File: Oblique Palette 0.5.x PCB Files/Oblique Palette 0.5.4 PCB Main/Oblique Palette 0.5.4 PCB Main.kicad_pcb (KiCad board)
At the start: 2 copper layers, 235 x 110 mm, 301 parts, among them J11 Conn_01x03_Male_Pin, J13 Conn_01x03_Male_Pin, J14 Conn_01x03_Male_Pin, J16 Conn_01x03_Female_Pin, J17 AudioJack2_SwitchT, J19 Conn_01x03_Female_Pin, J2 Conn_01x03_Male_Pin, J20 AudioJack2_SwitchT, J22 Conn_01x03_Female_Pin, J23 AudioJack2_SwitchT, J25 Conn_01x03_Female_Pin, J26 AudioJack2_SwitchT, J28 Conn_01x03_Female_Pin, J29 AudioJack2_SwitchT, J31 Conn_01x03_Female_Pin, J32 AudioJack2_SwitchT, J34 Conn_01x03_Female_Pin, J35 AudioJack2_SwitchT, J37 Conn_01x03_Female_Pin, J38 AudioJack2_SwitchT, J4 Conn_01x03_Male_Pin, J40 Conn_01x03_Female_Pin, J42 AudioJack2_SwitchT, J44 Conn_01x03_Female_Pin, J46 AudioJack2_SwitchT, J48 Conn_01x03_Female_Pin, J5 Conn_01x03_Male_Pin, J50 AudioJack2_SwitchT, J52 Conn_01x03_Female_Pin, J54 AudioJack2_SwitchT, J56 Conn_01x03_Female_Pin, J58 AudioJack2_SwitchT, J60 Conn_01x03_Female_Pin, J62 AudioJack2_SwitchT, J64 Conn_01x03_Female_Pin, J66 AudioJack2_SwitchT, J68 Conn_01x03_Female_Pin, J7 Conn_01x03_Male_Pin, J70 AudioJack2_SwitchT, J9 Conn_01x03_Male_Pin, U1 CD4051B, U10 MCP6004, U11 MCP4725xxx-xCH, U12 MCP6004, U13 MCP4725xxx-xCH, U14 MCP6004, U15 MCP4725xxx-xCH, U16 MCP6004, U17 MCP4725xxx-xCH, U18 MCP6004, U19 MCP4725xxx-xCH, U2 Pico, U20 MCP6004, U21 MCP4725xxx-xCH, U22 MCP6004, U23 MCP4725xxx-xCH, U24 MCP6004, U25 MCP4725xxx-xCH, U26 MCP6004, U3 MCP6004, U4 MCP6004, U5 MCP6004, U6 MCP6004, U7 MCP6004, U8 MCP6004, U9 MCP6004

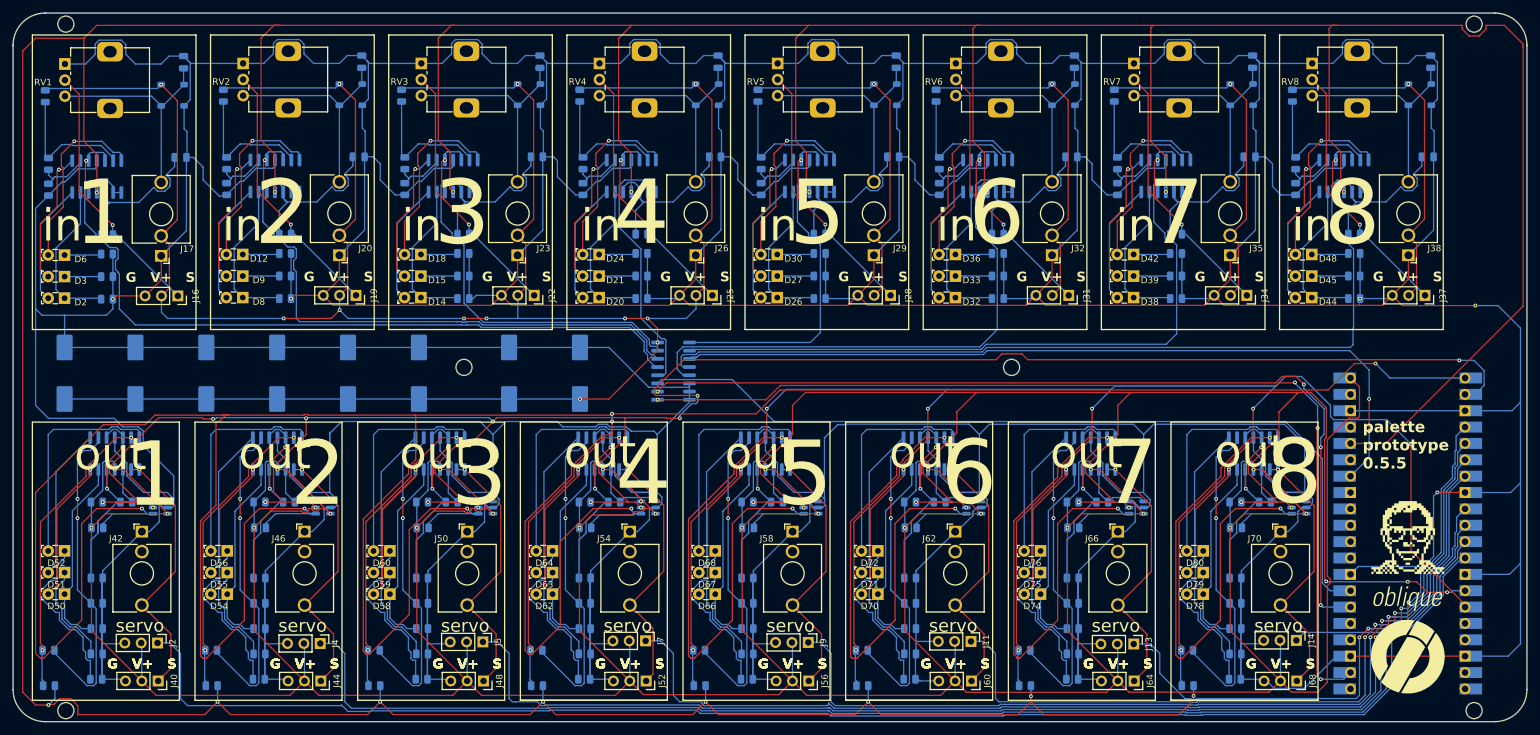
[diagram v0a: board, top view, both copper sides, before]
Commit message: Corrected missing traces but good.
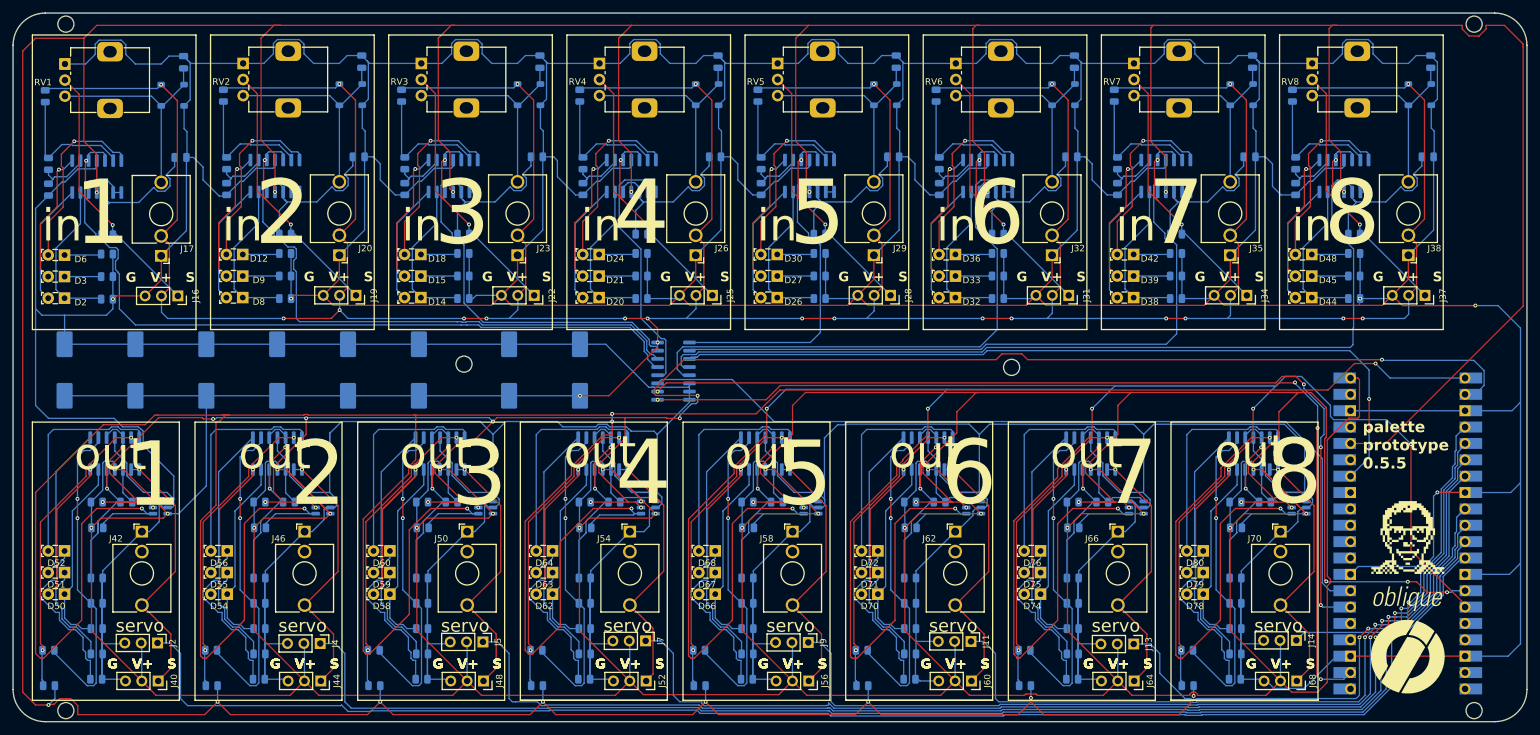
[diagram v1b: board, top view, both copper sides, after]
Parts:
- moved C1 0.50 mm to (103.0, 71.9)
- moved C2 0.50 mm to (56.0, 71.9)
- moved C3 0.50 mm to (92.0, 71.9)
- moved C4 0.50 mm to (45.0, 71.9)
- moved C5 0.50 mm to (78.0, 71.9)
- moved C6 0.50 mm to (34.0, 71.9)
- moved C7 0.50 mm to (67.0, 71.9)
- moved C8 0.50 mm to (23.0, 71.9)
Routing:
- net VCC: track 1468.9 -> 1617.2 mm, vias 43 -> 52
- net GNDREF: track 2153.2 -> 2154.0 mm
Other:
- outline, holes or cut-outs redrawn
